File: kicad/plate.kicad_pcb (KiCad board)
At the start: 2 copper layers, 125 x 85.3 mm, 21 parts, among them SW10 SW_PUSH, SW11 SW_PUSH, SW12 SW_PUSH, SW14 SW_PUSH, SW15 SW_PUSH, SW16 SW_PUSH, SW17 SW_PUSH, SW18 SW_PUSH, SW2 SW_PUSH, SW20 SW_PUSH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

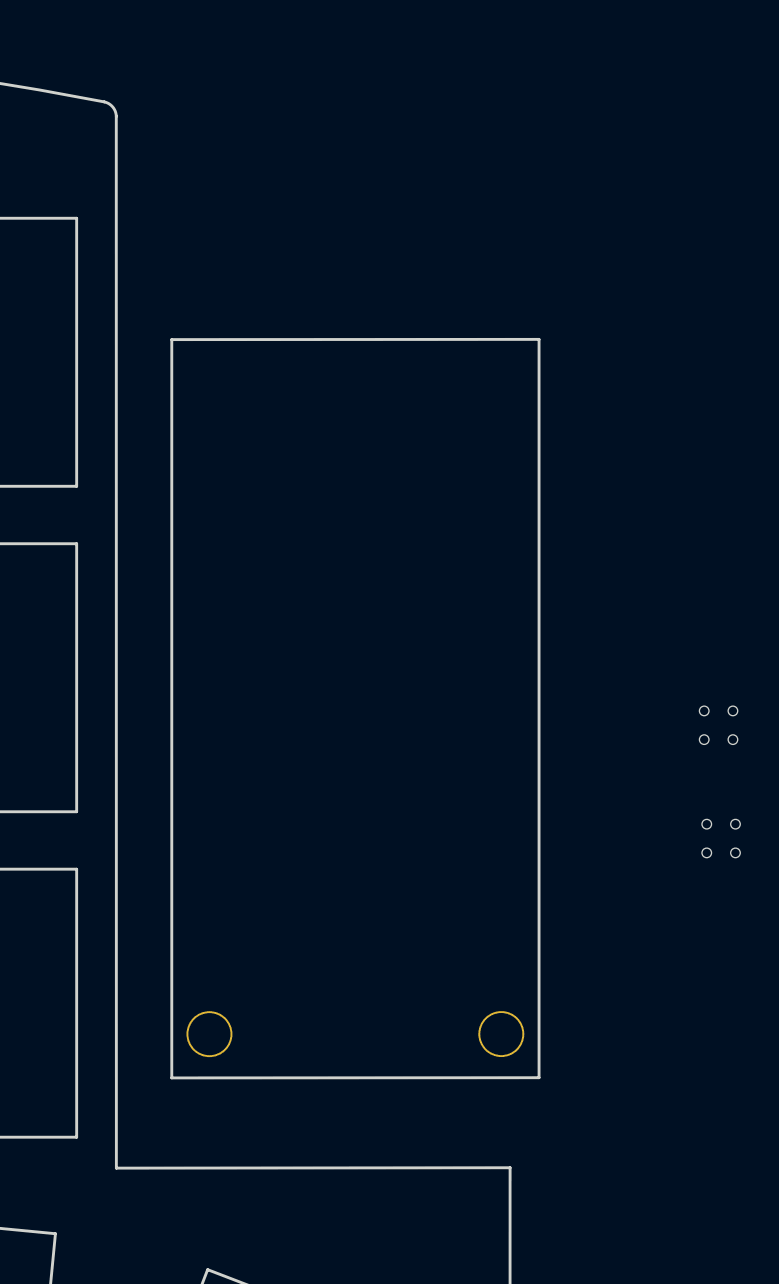
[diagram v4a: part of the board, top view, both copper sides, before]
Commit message: integrated mouse bite
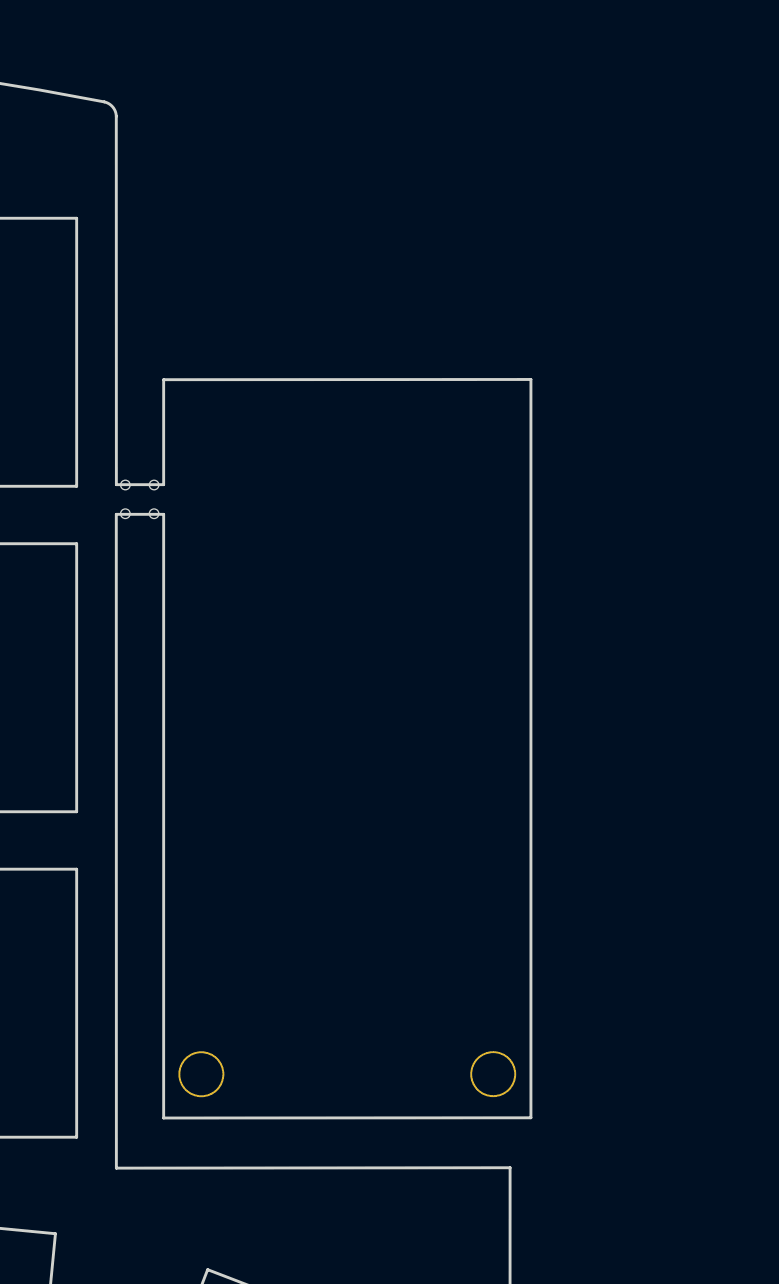
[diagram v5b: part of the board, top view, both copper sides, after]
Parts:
- removed the REF** at (222.1, 94.9)
- moved REF** 35.2 mm to (191.9, 83.1)
- moved h2 2.14 mm to (195.1, 113.1)
- moved h2 2.14 mm to (210.4, 113.1)
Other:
- board size 125 x 85.3 mm -> 124.6 x 85.3 mm
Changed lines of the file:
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@@
   )
   (net 0 "")
-  (footprint "broom:mouse-bite-2mm-slot-with-space-for-track" (layer "F.Cu")
-    (at 222.123 94.868 90)
-    (attr exclude_from_pos_files exclude_from_bom)
-    (fp_text reference "REF**" (at 0 -2 90) (layer "F.SilkS") hide
-      (effects (font (size 1 1) (thickness 0.2)))
-    )
-    (fp_text value "VAL**" (at 0 2.1 90) (layer "F.SilkS") hide
-      (effects (font (size 1 1) (thickness 0.2)))
-    )
-    (fp_arc (start -2 0) (end -2 -1) (angle 180) (layer "Dwgs.User") (width 0.1))
-    (fp_arc (start 2 0) (end 2 1) (angle 180) (layer "Dwgs.User") (width 0.1))
-    (fp_circle (center 2 0) (end 2.06 0) (layer "Dwgs.User") (width 0.05) (fill none))
-    (fp_circle (center -2 0) (end -2 -0.06) (layer "Dwgs.User") (width 0.05) (fill none))
-    (fp_line (start 2 0) (end 2 0) (layer "Eco1.User") (width 2))
-    (fp_line (start -2 0) (end -2 0) (layer "Eco1.User") (width 2))
-    (pad "" np_thru_hole circle locked (at -0.75 0.75 90) (size 0.5 0.5) (drill 0.5) (layers *.Cu *.Mask))
-    (pad "" np_thru_hole circle locked (at 0.75 -0.75 90) (size 0.5 0.5) (drill 0.5) (layers *.Cu *.Mask))
-    (pad "" np_thru_hole circle locked (at 0.75 0.75 90) (size 0.5 0.5) (drill 0.5) (layers *.Cu *.Mask))
-    (pad "" np_thru_hole circle locked (at -0.75 -0.75 90) (size 0.5 0.5) (drill 0.5) (layers *.Cu *.Mask))
-  )
   (footprint "broom:SW_PG1350_cut" (layer "F.Cu")
     (at 124.919 93.53 8)
@@
   )
   (footprint "chocorne:LEGO_HOLE" (layer "F.Cu")
-    (at 195.53 111.002)
+    (at 195.106 113.096)
     (descr "Mounting Hole 2.2mm, no annular, M2")
     (tags "mounting hole 2.2mm no annular m2")
@@
   )
   (footprint "broom:mouse-bite-2mm-slot-with-space-for-track" (layer "F.Cu")
-    (at 222.256 100.784 180)
+    (at 191.888 83.068 180)
     (attr exclude_from_pos_files exclude_from_bom)
     (fp_text reference "REF**" (at 0 -2) (layer "F.SilkS") hide
@@
   )
   (footprint "chocorne:LEGO_HOLE" (layer "F.Cu")
-    (at 210.775 110.997)
+    (at 210.351 113.091)
     (descr "Mounting Hole 2.2mm, no annular, M2")
     (tags "mounting hole 2.2mm no annular m2")
@@
     (fp_line (start 7 -7) (end 7 7) (layer "Edge.Cuts") (width 0.15))
   )
+  (gr_line (start 193.138 115.382) (end 193.138 83.85) (layer "Edge.Cuts") (width 0.15))
   (gr_arc (start 189.869405 63.084258) (end 190.664405 63.059258) (angle -75.82503188) (layer "Edge.Cuts") (width 0.15))
-  (gr_line (start 193.562 74.723) (end 212.746 74.712) (layer "Edge.Cuts") (width 0.15))
+  (gr_line (start 193.138 83.85) (end 190.667 83.85) (layer "Edge.Cuts") (width 0.15))
+  (gr_line (start 193.138 76.817) (end 212.322 76.806) (layer "Edge.Cuts") (width 0.15))
   (gr_line (start 211.234 117.98) (end 211.231003 128.040862) (layer "Edge.Cuts") (width 0.15))
-  (gr_line (start 190.669 118) (end 190.664405 63.059258) (layer "Edge.Cuts") (width 0.15))
-  (gr_line (start 193.562 113.288) (end 212.746 113.277) (layer "Edge.Cuts") (width 0.15))
+  (gr_line (start 190.669 82.3) (end 190.664405 63.059258) (layer "Edge.Cuts") (width 0.15))
+  (gr_line (start 190.669 118) (end 190.664405 83.85) (layer "Edge.Cuts") (width 0.15))
+  (gr_line (start 193.138 115.382) (end 212.322 115.371) (layer "Edge.Cuts") (width 0.15))
   (gr_line (start 88.127953 83.292666) (end 105.361412 136.251738) (layer "Edge.Cuts") (width 0.15))
-  (gr_line (start 193.562 113.288) (end 193.562 74.723) (layer "Edge.Cuts") (width 0.15))
+  (gr_line (start 193.138 82.3) (end 193.138 76.817) (layer "Edge.Cuts") (width 0.15))
   (gr_arc (start 155.4857 240.406359) (end 190.039849 62.307342) (angle -30.52241692) (layer "Edge.Cuts") (width 0.15))
   (gr_arc (start 188.968743 128.55) (end 206.239908 142.606113) (angle -40.45049692) (layer "Edge.Cuts") (width 0.15))
   (gr_arc (start 99.626551 80.295466) (end 94.799583 69.437227) (angle -80.64225145) (layer "Edge.Cuts") (width 0.15))
+  (gr_line (start 193.138 82.3) (end 190.669 82.3) (layer "Edge.Cuts") (width 0.15))
   (gr_arc (start 141.689 320.542281) (end 106.709135 136.975628) (angle 18.02701016) (layer "Edge.Cuts") (width 0.15))
   (gr_arc (start 135.189 334.05) (end 165.233781 135.161726) (angle 10.5566717) (layer "Edge.Cuts") (width 0.15))
-  (gr_line (start 212.746 113.277) (end 212.746 74.712) (layer "Edge.Cuts") (width 0.15))
+  (gr_line (start 212.322 115.371) (end 212.322 76.806) (layer "Edge.Cuts") (width 0.15))
   (gr_arc (start 202.695496 139.738695) (end 201.163167 144.032518) (angle -70.66711935) (layer "Edge.Cuts") (width 0.15))
   (gr_arc (start 106.46079 135.821466) (end 105.361412 136.251738) (angle -80.76911852) (layer "Edge.Cuts") (width 0.15))
   (gr_line (start 190.669 118) (end 211.234 117.98) (layer "Edge.Cuts") (width 0.15))
-  (group "" (id a308bf8a-7b15-4c69-8d2d-f307d8baa6de)
-    (members
-      2600aef0-55e7-486c-97a5-7d49fb7776f9
-      47053596-ba74-48b3-a822-1d2797a26388
-      60d902c8-7d9d-4d47-ae0f-074e021be140
-      8520a7a4-f90c-4619-9e30-1e98949422c4
-      8a669e94-7038-46fd-9b70-906083bff600
-      e733b390-f7c4-44db-8681-523d96046aea
-    )
-  )
 )

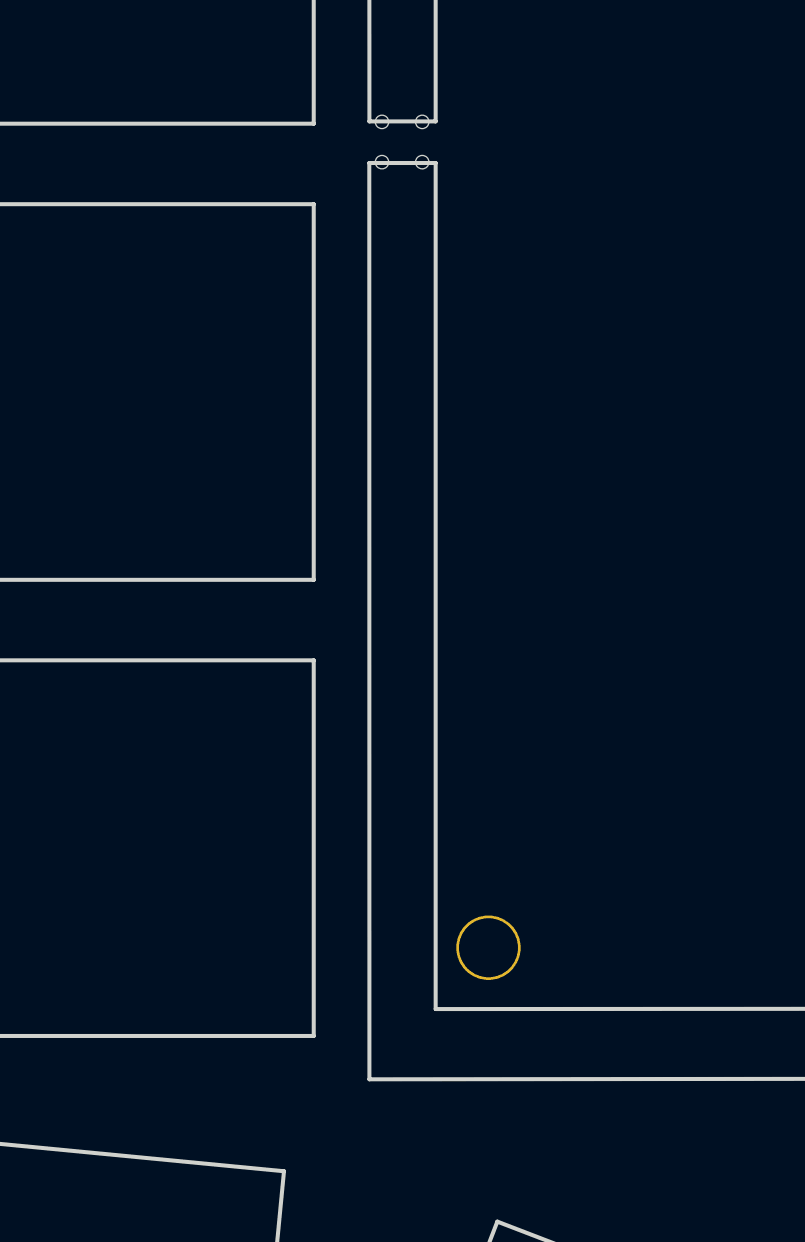
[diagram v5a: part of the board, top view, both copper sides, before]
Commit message: integrated mouse bite - dual bridge
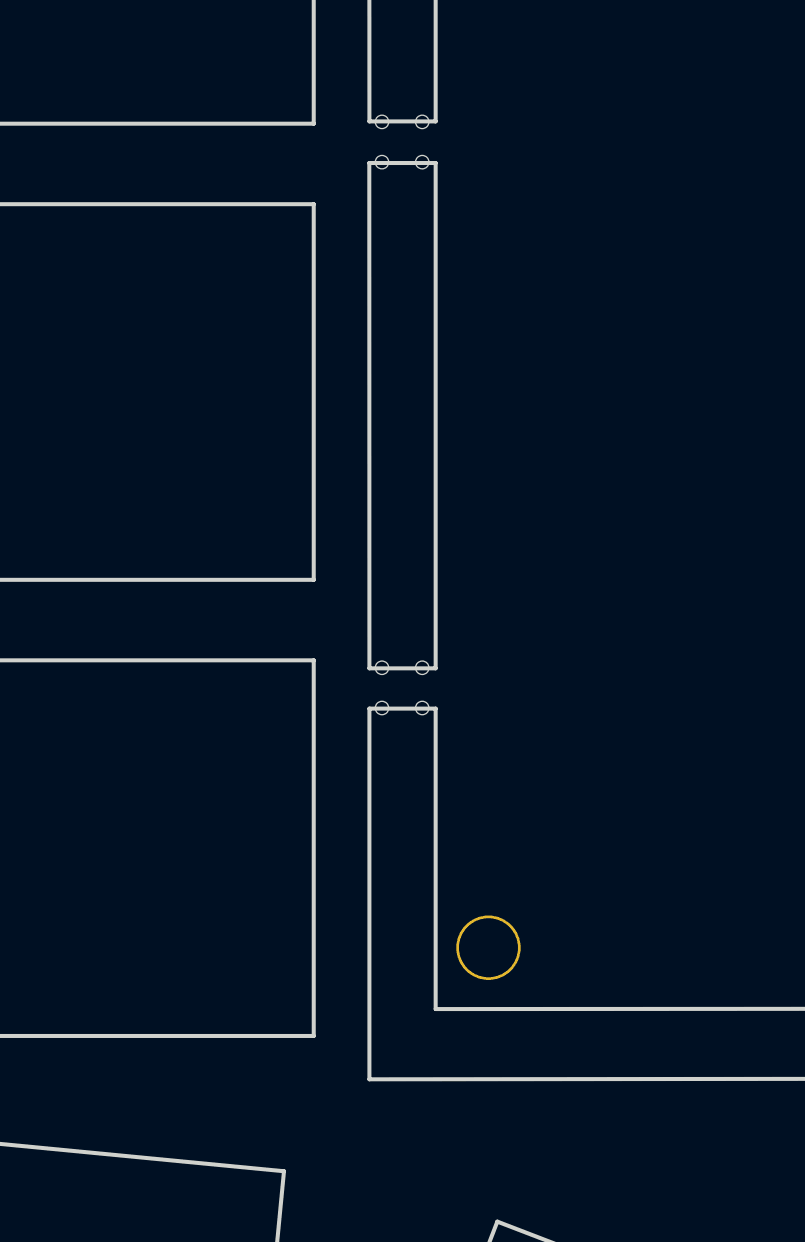
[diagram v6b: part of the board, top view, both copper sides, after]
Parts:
- added REF**: VAL**, broom:mouse-bite-2mm-slot-with-space-for-track, F.Cu at (191.9, 103.4)
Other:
- outline, holes or cut-outs redrawn
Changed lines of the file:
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@@
     (pad "h2" thru_hole circle locked (at 0 0) (size 2.4 2.4) (drill 2.2) (layers *.Cu *.Mask))
+  )
+  (footprint "broom:mouse-bite-2mm-slot-with-space-for-track" (layer "F.Cu")
+    (at 191.888 103.412 180)
+    (attr exclude_from_pos_files exclude_from_bom)
+    (fp_text reference "REF**" (at 0 -2) (layer "F.SilkS") hide
+      (effects (font (size 1 1) (thickness 0.2)))
+    )
+    (fp_text value "VAL**" (at 0 2.1) (layer "F.SilkS") hide
+      (effects (font (size 1 1) (thickness 0.2)))
+    )
+    (fp_arc (start 2 0) (end 2 1) (angle 180) (layer "Dwgs.User") (width 0.1))
+    (fp_arc (start -2 0) (end -2 -1) (angle 180) (layer "Dwgs.User") (width 0.1))
+    (fp_circle (center -2 0) (end -2 -0.06) (layer "Dwgs.User") (width 0.05) (fill none))
+    (fp_circle (center 2 0) (end 2.06 0) (layer "Dwgs.User") (width 0.05) (fill none))
+    (fp_line (start 2 0) (end 2 0) (layer "Eco1.User") (width 2))
+    (fp_line (start -2 0) (end -2 0) (layer "Eco1.User") (width 2))
+    (pad "" np_thru_hole circle locked (at 0.75 0.75 180) (size 0.5 0.5) (drill 0.5) (layers *.Cu *.Mask))
+    (pad "" np_thru_hole circle locked (at -0.75 0.75 180) (size 0.5 0.5) (drill 0.5) (layers *.Cu *.Mask))
+    (pad "" np_thru_hole circle locked (at -0.75 -0.75 180) (size 0.5 0.5) (drill 0.5) (layers *.Cu *.Mask))
+    (pad "" np_thru_hole circle locked (at 0.75 -0.75 180) (size 0.5 0.5) (drill 0.5) (layers *.Cu *.Mask))
   )
   (footprint "broom:SW_PG1350_cut" (layer "F.Cu")
@@
     (fp_line (start 7 -7) (end 7 7) (layer "Edge.Cuts") (width 0.15))
   )
-  (gr_line (start 193.138 115.382) (end 193.138 83.85) (layer "Edge.Cuts") (width 0.15))
+  (gr_line (start 193.138 115.382) (end 193.138 104.184) (layer "Edge.Cuts") (width 0.15))
   (gr_arc (start 189.869405 63.084258) (end 190.664405 63.059258) (angle -75.82503188) (layer "Edge.Cuts") (width 0.15))
+  (gr_line (start 193.138 104.184) (end 190.669 104.184) (layer "Edge.Cuts") (width 0.15))
+  (gr_line (start 193.138 102.684) (end 190.669 102.684) (layer "Edge.Cuts") (width 0.15))
   (gr_line (start 193.138 83.85) (end 190.667 83.85) (layer "Edge.Cuts") (width 0.15))
   (gr_line (start 193.138 76.817) (end 212.322 76.806) (layer "Edge.Cuts") (width 0.15))
+  (gr_line (start 193.138 102.684) (end 193.138 83.85) (layer "Edge.Cuts") (width 0.15))
   (gr_line (start 211.234 117.98) (end 211.231003 128.040862) (layer "Edge.Cuts") (width 0.15))
   (gr_line (start 190.669 82.3) (end 190.664405 63.059258) (layer "Edge.Cuts") (width 0.15))
-  (gr_line (start 190.669 118) (end 190.664405 83.85) (layer "Edge.Cuts") (width 0.15))
+  (gr_line (start 190.669 118) (end 190.669 104.184) (layer "Edge.Cuts") (width 0.15))
   (gr_line (start 193.138 115.382) (end 212.322 115.371) (layer "Edge.Cuts") (width 0.15))
   (gr_line (start 88.127953 83.292666) (end 105.361412 136.251738) (layer "Edge.Cuts") (width 0.15))
@@
   (gr_arc (start 155.4857 240.406359) (end 190.039849 62.307342) (angle -30.52241692) (layer "Edge.Cuts") (width 0.15))
   (gr_arc (start 188.968743 128.55) (end 206.239908 142.606113) (angle -40.45049692) (layer "Edge.Cuts") (width 0.15))
+  (gr_line (start 190.669 102.684) (end 190.664405 83.85) (layer "Edge.Cuts") (width 0.15))
   (gr_arc (start 99.626551 80.295466) (end 94.799583 69.437227) (angle -80.64225145) (layer "Edge.Cuts") (width 0.15))
   (gr_line (start 193.138 82.3) (end 190.669 82.3) (layer "Edge.Cuts") (width 0.15))

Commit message: Add plate
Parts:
- added  : LOGO, broom:happy, F.Cu at (172.7, 91.0)
- added  : LOGO, broom:cat, F.Cu at (161.7, 125.9)
